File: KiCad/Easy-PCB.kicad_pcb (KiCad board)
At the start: 2 copper layers, 177.8 x 83.8 mm, 99 parts, among them J1 703W-00/53, J3 HLW20R-2C7LF, K1 G5LE-1A-E_DC12, P1 1x02, P12 M20-9980346, P2 1x06, P24 M20-9980346, P3 1x04, P4 1x03 Terminal Block, P5 1x02, P6 via, P7 via, Q1 2N3904, Q10 MJE350, Q11 2N3904, Q12 2N3904, Q13 MJE340, Q14 MJE350, Q15 2N3904, Q16 MJE340, Q17 MJE350, Q18 2N3904, Q19 2N3904, Q2 MJE340, Q3 2N3904, Q4 2N3904, Q5 MJE340, Q6 MJE350, Q7 2N3904, Q8 2N3904, Q9 MJE340, SW1 R1966ABLKBLKFR, T1 VPP24-830, U1 PIC16F883, U2 MCP41050, U3 MCP617, U4 MCP9700A, U5 LM7805

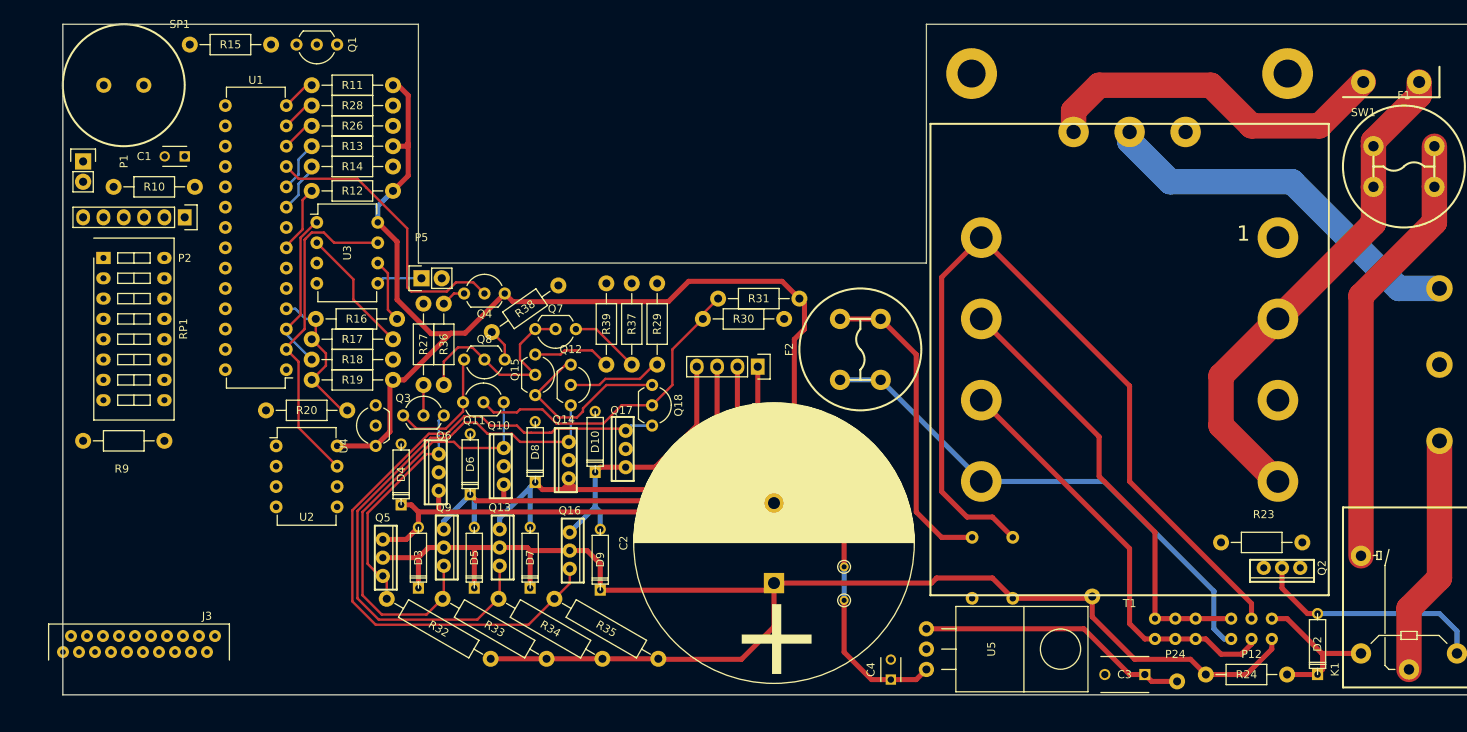
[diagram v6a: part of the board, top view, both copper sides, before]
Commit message: connector to front PCB routed
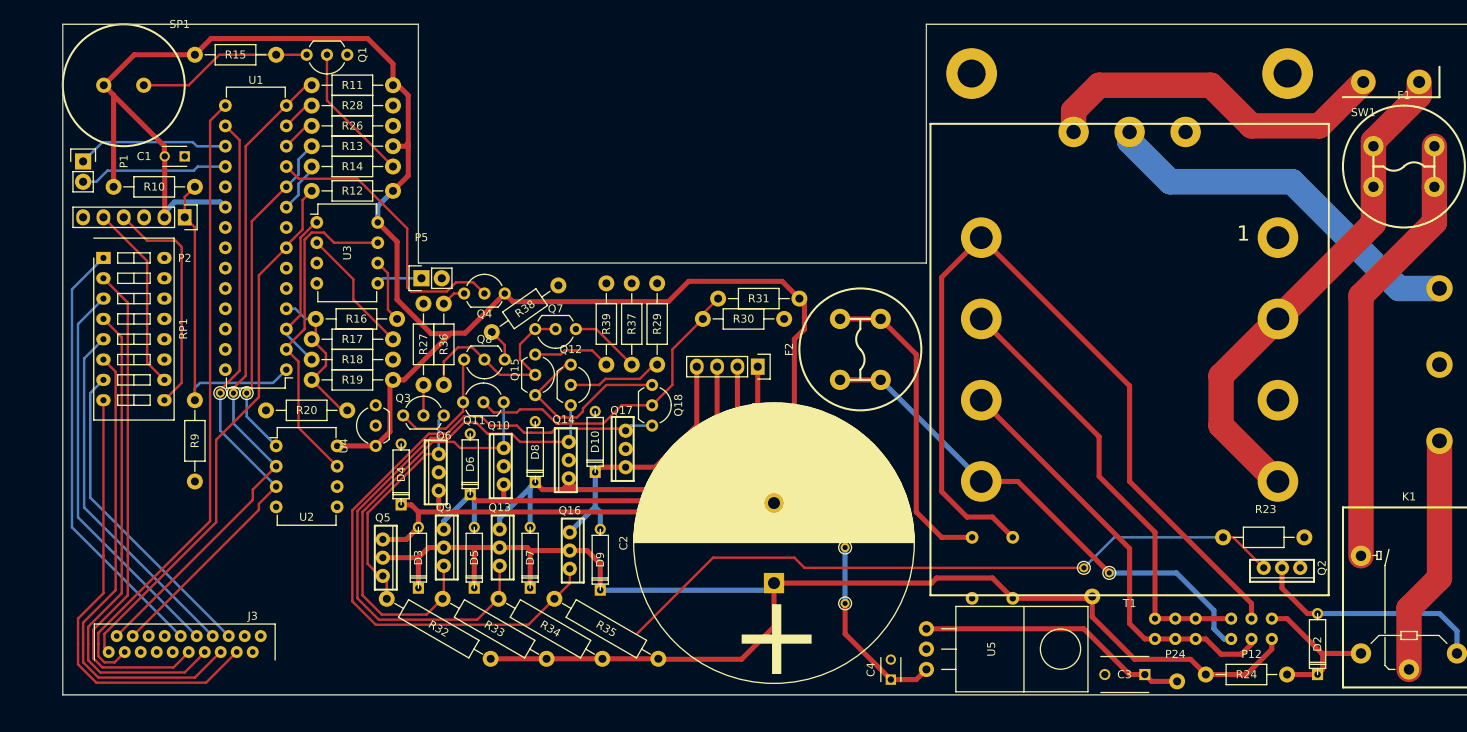
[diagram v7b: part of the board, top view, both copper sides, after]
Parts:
- added P10: via, Connect:PINTST, F.Cu at (70.5, 84.2)
- added P11: via, Connect:PINTST, F.Cu at (72.1, 84.2)
- added P13: via, Connect:PINTST, F.Cu at (73.8, 84.2)
- added P8: via, Connect:PINTST, F.Cu at (181.6, 106.7)
- added P9: via, Connect:PINTST, F.Cu at (178.4, 106.0)
- moved R9 8.89 mm to (67.3, 90.2), turned to 270 degrees
- moved J3 5.72 mm to (66.0, 115.6)
- moved P7 2.42 mm to (148.6, 103.5)
- moved Q1 1.80 mm to (86.4, 41.9)
- moved R15 1.42 mm to (72.4, 41.9)
- moved R23 0.68 mm to (200.9, 102.2)
- moved P6 0.40 mm to (148.6, 110.5)
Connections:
- net /Heat Relay/DoorC2 renamed DoorC2
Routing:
- net DoorC2: track 0.00 -> 86.0 mm
- net VDD: track 172.8 -> 254.1 mm
- net MISO: track 0.00 -> 79.6 mm
- net SCK: track 4.23 -> 83.7 mm
- net MOSI: track 0.00 -> 75.8 mm
- net Net-(J3-Pad11): track 0.00 -> 63.8 mm
- net Net-(J3-Pad13): track 0.00 -> 61.6 mm
- net CS1: track 8.43 -> 68.6 mm
- net Net-(J3-Pad15): track 0.00 -> 59.5 mm
- net Net-(J3-Pad17): track 0.00 -> 56.7 mm
- net Net-(J3-Pad10): track 0.00 -> 54.5 mm
- net Net-(J3-Pad12): track 0.00 -> 49.6 mm
- net Net-(J3-Pad14): track 0.00 -> 44.8 mm
- net Net-(P2-Pad1): track 0.00 -> 41.6 mm
- net Net-(J3-Pad16): track 0.00 -> 39.9 mm
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
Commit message: routing complete
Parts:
- added P14: via, Connect:PINTST, F.Cu at (67.6, 106.7)
- added P15: via, Connect:PINTST, F.Cu at (88.6, 82.3)
- added P16: via, Connect:PINTST, F.Cu at (92.6, 70.9)
- added P17: via, Connect:PINTST, F.Cu at (100.2, 75.2)
- added P18: via, Connect:PINTST, F.Cu at (66.0, 50.5)
- added P19: via, Connect:PINTST, F.Cu at (67.6, 82.8)
- moved R21 108.9 mm to (80.0, 88.3), turned to 180 degrees
- moved C7 107.9 mm to (67.7, 86.0), turned to 270 degrees
- moved C5 97.3 mm to (86.7, 119.4)
- moved C8 86.9 mm to (68.6, 95.1)
- moved C6 82.2 mm to (70.9, 109.3), turned to 90 degrees
- moved R45 78.7 mm to (66.9, 102.0)
- moved R22 78.7 mm to (78.7, 114.3), turned to 90 degrees
- moved R44 76.6 mm to (91.6, 115.6), turned to 350 degrees
- moved R41 75.1 mm to (88.1, 102.6), turned to 270 degrees
- moved R43 68.7 mm to (83.8, 114.3), turned to 90 degrees
- moved R42 66.4 mm to (74.7, 105.4), turned to 90 degrees
- moved R46 61.9 mm to (65.5, 94.2), turned to 90 degrees
- moved R40 60.1 mm to (81.3, 114.3), turned to 270 degrees
- moved R47 59.6 mm to (63.0, 94.2), turned to 270 degrees
- moved Q19 55.5 mm to (77.5, 106.0)
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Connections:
- net /Motor Driver/Motor_On renamed Motor_On
- net Net-(P2-Pad1) renamed Reset
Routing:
- net VDD: track 254.1 -> 423.2 mm
- net /Analog Math/NichromeTemp: track 0.00 -> 63.4 mm
- net Net-(Q12-Pad2): track 11.8 -> 72.9 mm
- net DoorC2: track 86.0 -> 137.7 mm
- net /Heat Relay/Heat: track 0.00 -> 44.9 mm
- net Net-(Q3-Pad2): track 3.81 -> 42.6 mm
- net GND: track 0.00 -> 33.7 mm, vias 0 -> 1
- net Net-(R16-Pad2): track 7.98 -> 36.3 mm
- net Net-(U3-Pad3): track 0.00 -> 27.7 mm
- net Net-(Q16-Pad3): track 87.5 -> 61.0 mm
- net Net-(C6-Pad2): track 0.00 -> 25.9 mm
- net Net-(J3-Pad18): track 0.00 -> 22.8 mm
- net Net-(C7-Pad2): track 0.00 -> 19.8 mm
- net Net-(Q19-Pad2): track 0.00 -> 19.4 mm
- net Net-(C8-Pad2): track 0.00 -> 12.3 mm
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- added copper zone on B.Cu, net GND
